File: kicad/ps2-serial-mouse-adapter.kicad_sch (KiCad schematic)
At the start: 12 parts, among them U1 Arduino_Mini, U2 MAX232

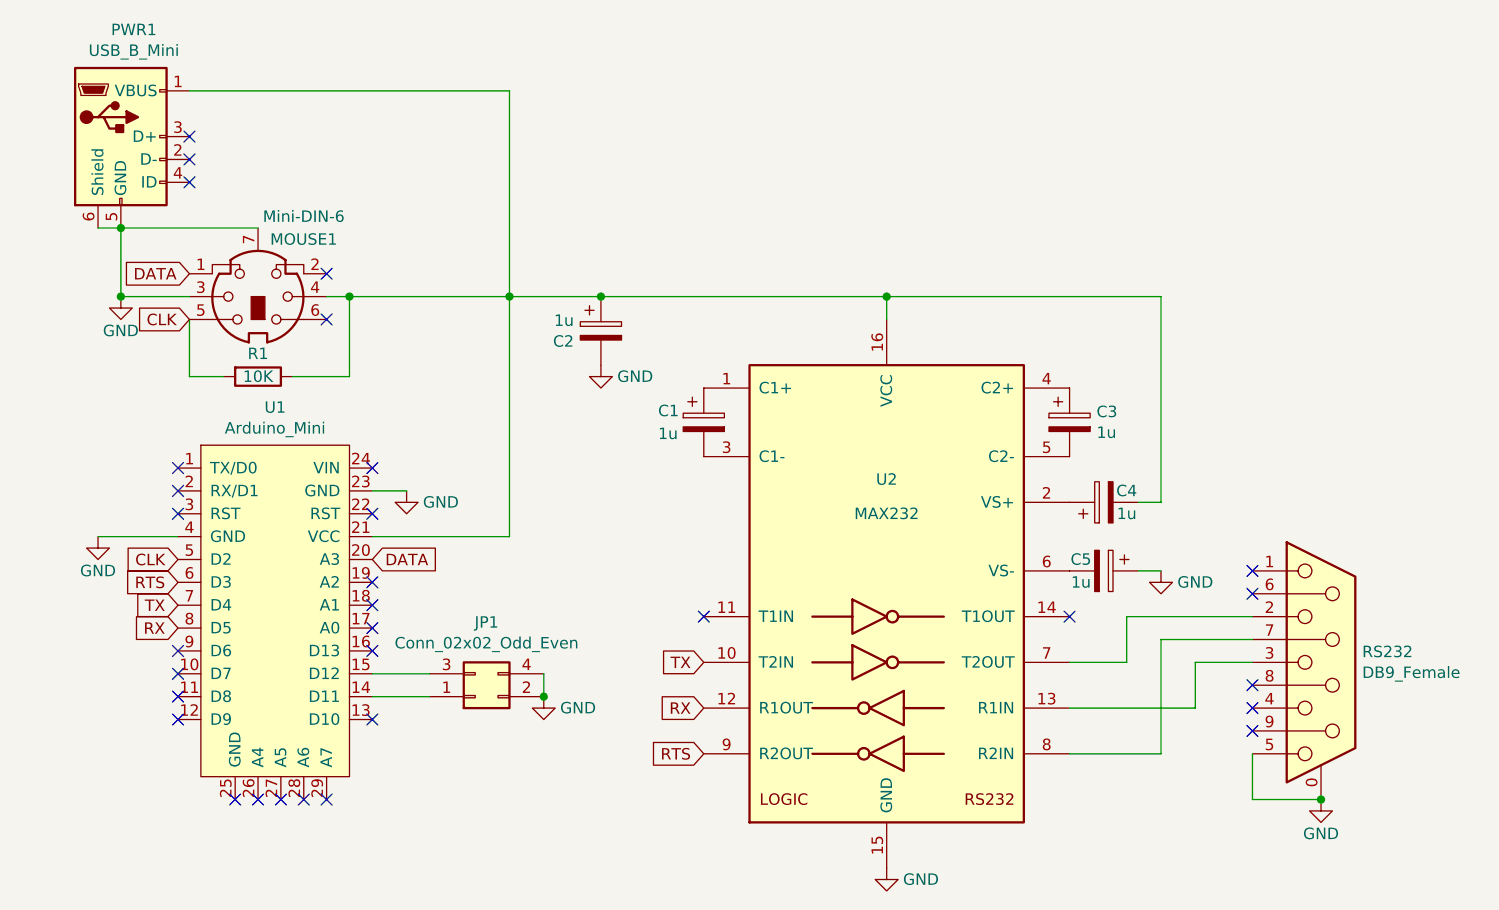
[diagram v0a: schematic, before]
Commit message: Add footprints for Arduino Nano socket and MAX3232 HW-027 module
- Created a new footprint for the Arduino Nano socket with 2x15 pin configuration, including through-hole pads and silk screen details.
- Added a footprint for the MAX3232 HW-027 module featuring castellated pads, through-hole and SMD pads, along with necessary fabrication outlines.
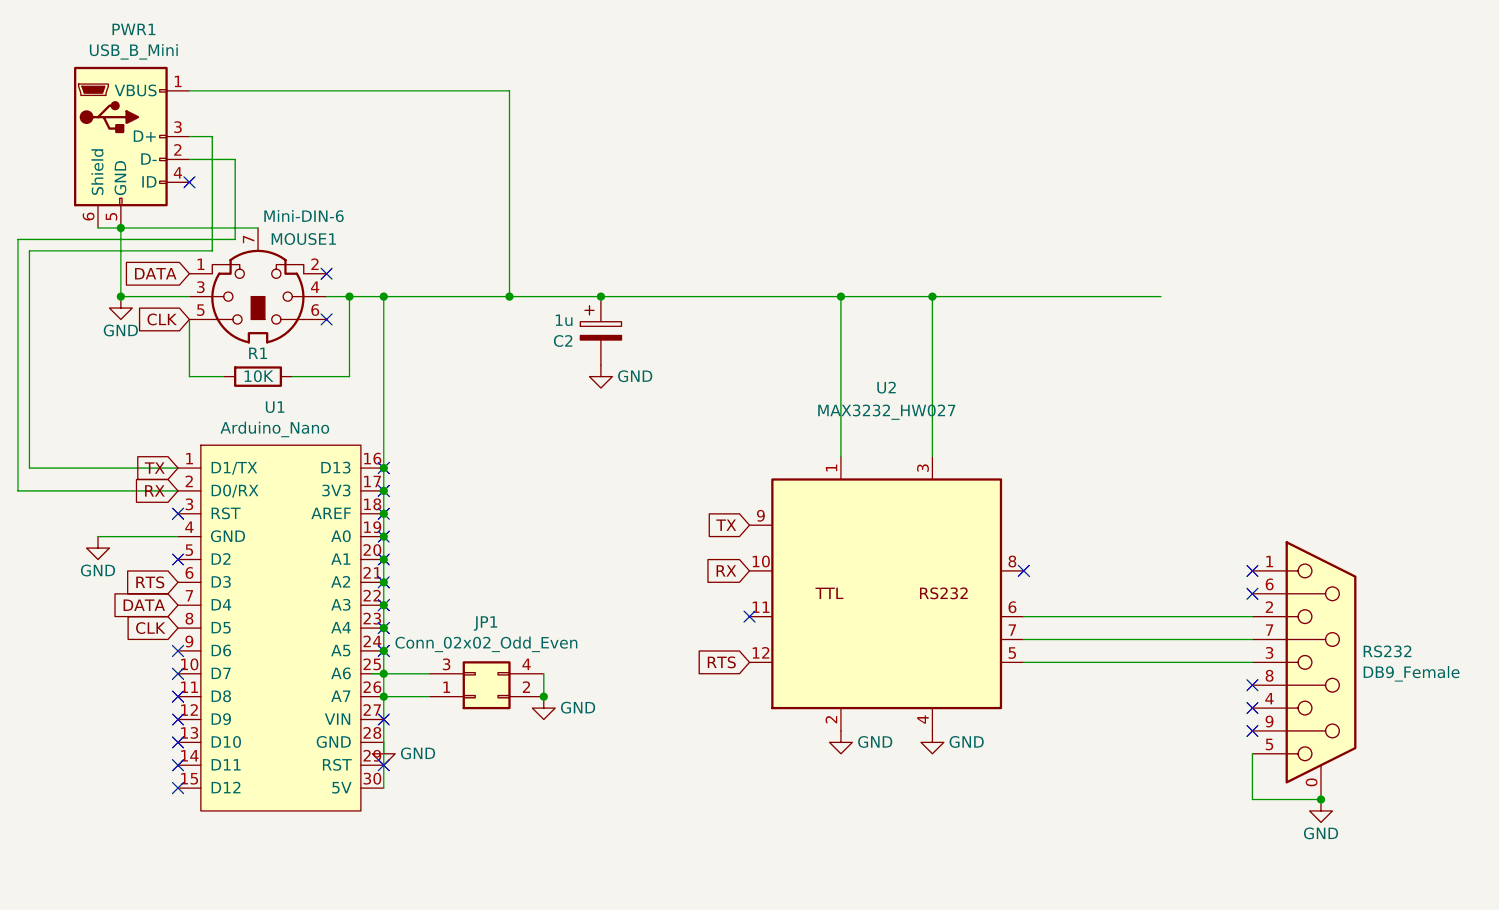
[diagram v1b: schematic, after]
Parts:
- removed C1, C3, C4, C5: 1u, Capacitor_THT:CP_Radial_D4.0mm_P1.50mm, symbol ps2-serial-mouse-adapter-rescue:CP-Device
- U1: value Arduino_Mini -> Arduino_Nano; footprint Package_DIP:DIP-24_W15.24mm_Socket -> ps2-serial-mouse-adapter:Arduino_Nano_Socket; symbol ps2-serial-mouse-adapter:Arduino_Mini -> ps2-serial-mouse-adapter:Arduino_Nano
- U2: value MAX232 -> MAX3232_HW027; footprint Package_DIP:DIP-16_W7.62mm_Socket -> ps2-serial-mouse-adapter:MAX3232_HW027; symbol Interface_UART:MAX232 -> ps2-serial-mouse-adapter:MAX3232_HW027; LCSC Part C911187 -> (none)
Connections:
- net CLK: now also U1.8 (D5); no longer U1.5 (D2)
- net DATA: now also U1.7 (D4); no longer U1.20 (A3)
- net GND: now also U1.28 (GND), U2.2 (GND), U2.4 (GND2); no longer U1.23 (GND), U2.15 (GND)
- net RTS: now also U2.12 (TTL_RXD2); no longer U2.9 (R2OUT)
- net RX: now also PWR1.2 (D-), U1.2 (D0/RX), U2.10 (TTL_RXD1); no longer U1.8 (D5), U2.12 (R1OUT)
- net TX: now also PWR1.3 (D+), U1.1 (D1/TX), U2.9 (TTL_TXD1); no longer U1.7 (D4), U2.10 (T2IN)
- net at U1.14 (D11): no longer JP1.1 (Pin_1)
- net at U1.15 (D12): no longer JP1.3 (Pin_3)
- net at U1.16 (D13): now also C2.1, JP1.1 (Pin_1), JP1.3 (Pin_3), MOUSE1.4, PWR1.1 (VBUS), R1.1, U1.17 (3V3), U1.18 (AREF), U1.19 (A0), U1.20 (A1), U1.21 (A2), U1.22 (A3), U1.23 (A4), U1.24 (A5), U1.25 (A6), U1.26 (A7), U1.30 (5V), U2.1 (VCC), U2.3 (VCC2)
- net at RS232.3: now also U2.5 (RS232_RXD1); no longer U2.13 (R1IN)
- net at U2.6 (RS232_TXD1): now also RS232.2
- net at U2.7 (RS232_RXD2): now also RS232.7; no longer RS232.2
- net at U2.8 (RS232_TXD2): no longer RS232.7
- no-connect marks 31 -> 30
